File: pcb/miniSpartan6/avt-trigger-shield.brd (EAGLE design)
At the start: 52.1 x 76.2 mm, 20 parts

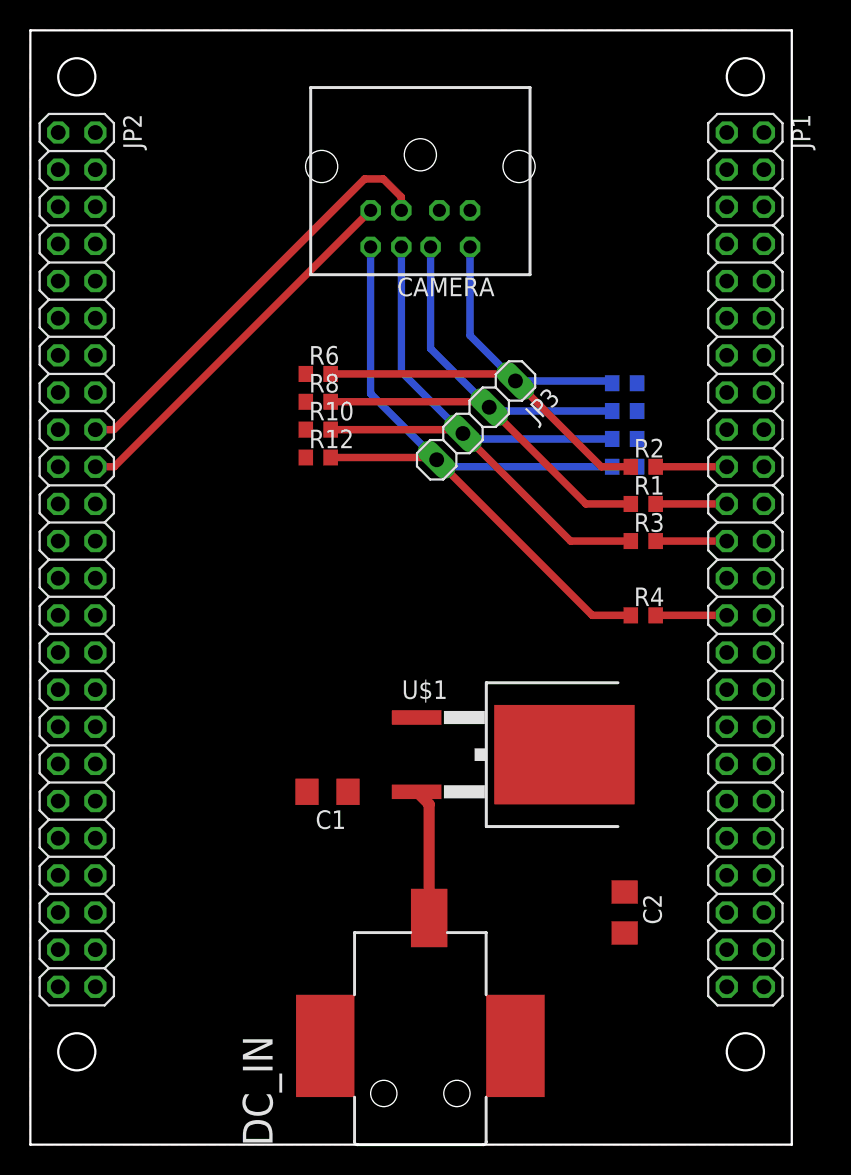
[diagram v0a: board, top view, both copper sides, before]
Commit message: finished avt trigger board
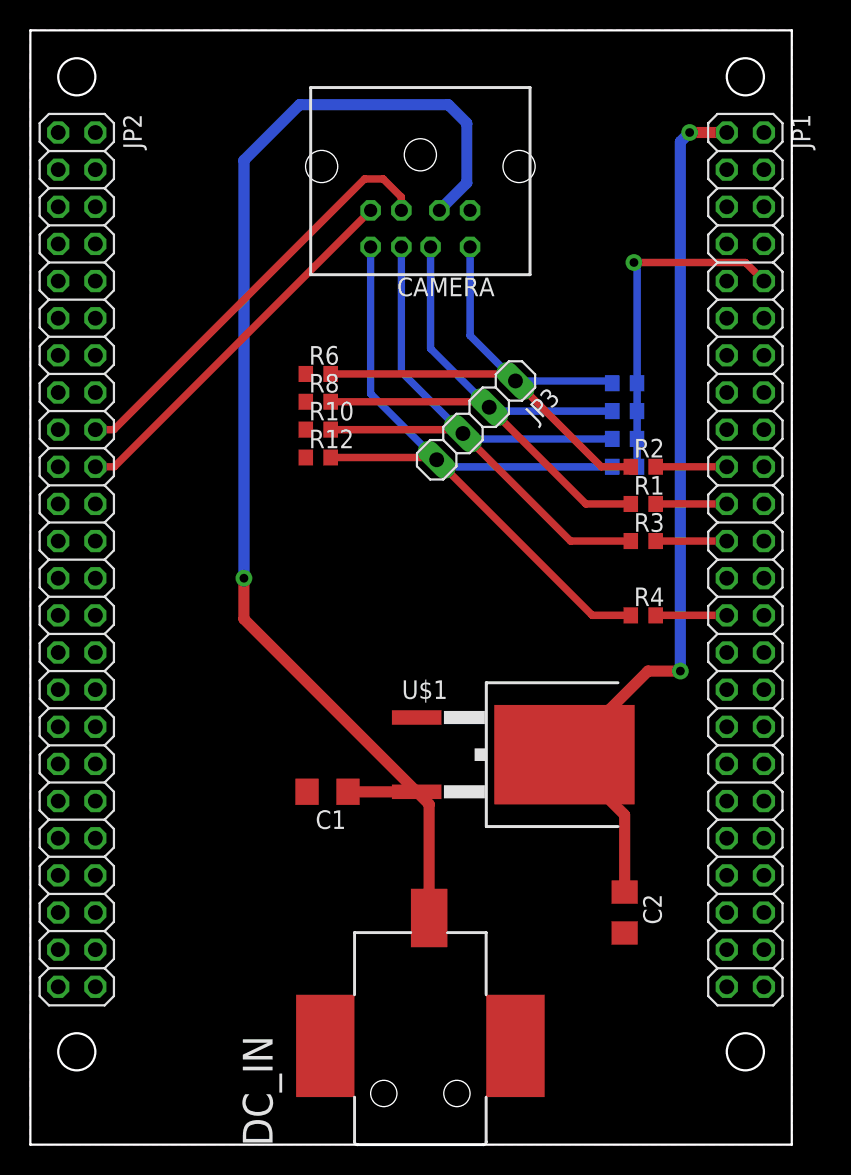
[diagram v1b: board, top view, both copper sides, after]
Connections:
- net 3V3: now also JP1.10
- net GND: now also JP2.47, JP2.48
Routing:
- net VIN: track 8.98 -> 85.8 mm, vias 0 -> 1
- net VCC: track 0.00 -> 61.0 mm, vias 0 -> 2
- net 3V3: track 0.00 -> 23.5 mm, vias 0 -> 1
- added copper zone on layer 16, net GND
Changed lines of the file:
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@@
 <wire x1="27.27" y1="15.5" x2="27.27" y2="23.28" width="0.762" layer="1"/>
 <wire x1="27.27" y1="23.28" x2="26.42" y2="24.13" width="0.762" layer="1"/>
-<wire x1="26.42" y1="24.13" x2="27.97" y2="63.89" width="0" layer="19" extent="1-1"/>
-<wire x1="21.72" y1="24.13" x2="26.42" y2="24.13" width="0" layer="19" extent="1-1"/>
+<wire x1="26.42" y1="24.13" x2="21.72" y2="24.13" width="0.762" layer="1"/>
+<wire x1="26.42" y1="24.13" x2="14.605" y2="35.945" width="0.762" layer="1"/>
+<wire x1="14.605" y1="35.945" x2="14.605" y2="38.735" width="0.762" layer="1"/>
+<via x="14.605" y="38.735" extent="1-16" drill="0.6" diameter="1.15"/>
+<wire x1="14.605" y1="38.735" x2="14.605" y2="67.31" width="0.762" layer="16"/>
+<wire x1="14.605" y1="67.31" x2="18.415" y2="71.12" width="0.762" layer="16"/>
+<wire x1="18.415" y1="71.12" x2="28.575" y2="71.12" width="0.762" layer="16"/>
+<wire x1="28.575" y1="71.12" x2="29.845" y2="69.85" width="0.762" layer="16"/>
+<wire x1="29.845" y1="65.765" x2="27.97" y2="63.89" width="0.762" layer="16"/>
+<wire x1="29.845" y1="69.85" x2="29.845" y2="65.765" width="0.762" layer="16"/>
 </signal>
 <signal name="GND">
@@
 <contactref element="R10" pad="1"/>
 <contactref element="R12" pad="1"/>
+<polygon width="0.762" layer="16" isolate="0.508">
+<vertex x="0" y="76.2"/>
+<vertex x="52.07" y="76.2"/>
+<vertex x="52.07" y="0"/>
+<vertex x="0" y="0"/>
+</polygon>
+<contactref element="JP2" pad="47"/>
+<contactref element="JP2" pad="48"/>
 </signal>
 <signal name="VCC">
@@
 <contactref element="JP1" pad="1"/>
 <contactref element="C2" pad="1"/>
-<wire x1="36.52" y1="26.67" x2="47.625" y2="69.215" width="0" layer="19" extent="1-1"/>
-<wire x1="40.64" y1="17.275" x2="36.52" y2="26.67" width="0" layer="19" extent="1-1"/>
+<wire x1="36.52" y1="26.67" x2="40.64" y2="22.55" width="0.762" layer="1"/>
+<wire x1="40.64" y1="22.55" x2="40.64" y2="17.275" width="0.762" layer="1"/>
+<wire x1="36.52" y1="26.67" x2="42.235" y2="32.385" width="0.762" layer="1"/>
+<wire x1="42.235" y1="32.385" x2="44.45" y2="32.385" width="0.762" layer="1"/>
+<via x="44.45" y="32.385" extent="1-16" drill="0.6" diameter="1.15"/>
+<wire x1="44.45" y1="32.385" x2="44.45" y2="68.58" width="0.762" layer="16"/>
+<wire x1="44.45" y1="68.58" x2="45.085" y2="69.215" width="0.762" layer="16"/>
+<via x="45.085" y="69.215" extent="1-16" drill="0.6" diameter="1.15"/>
+<wire x1="45.085" y1="69.215" x2="47.625" y2="69.215" width="0.762" layer="1"/>
 </signal>
 <signal name="TX">
@@
 <contactref element="R7" pad="2"/>
 <contactref element="R9" pad="2"/>
-<wire x1="41.49" y1="50.165" x2="41.49" y2="52.07" width="0" layer="19" extent="16-16"/>
-<wire x1="41.49" y1="48.26" x2="41.49" y2="50.165" width="0" layer="19" extent="16-16"/>
-<wire x1="41.49" y1="46.355" x2="41.49" y2="48.26" width="0" layer="19" extent="16-16"/>
+<wire x1="41.49" y1="52.07" x2="41.49" y2="50.165" width="0.508" layer="16"/>
+<wire x1="41.49" y1="50.165" x2="41.49" y2="48.26" width="0.508" layer="16"/>
+<wire x1="41.49" y1="48.26" x2="41.49" y2="46.355" width="0.508" layer="16"/>
+<contactref element="JP1" pad="10"/>
+<wire x1="50.165" y1="59.055" x2="48.895" y2="60.325" width="0.508" layer="1"/>
+<wire x1="48.895" y1="60.325" x2="41.275" y2="60.325" width="0.508" layer="1"/>
+<via x="41.275" y="60.325" extent="1-16" drill="0.6" diameter="1.15"/>
+<wire x1="41.275" y1="60.325" x2="41.49" y2="60.11" width="0.508" layer="16"/>
+<wire x1="41.49" y1="60.11" x2="41.49" y2="52.07" width="0.508" layer="16"/>
 </signal>
 </signals>

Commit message: fixed pin assignments
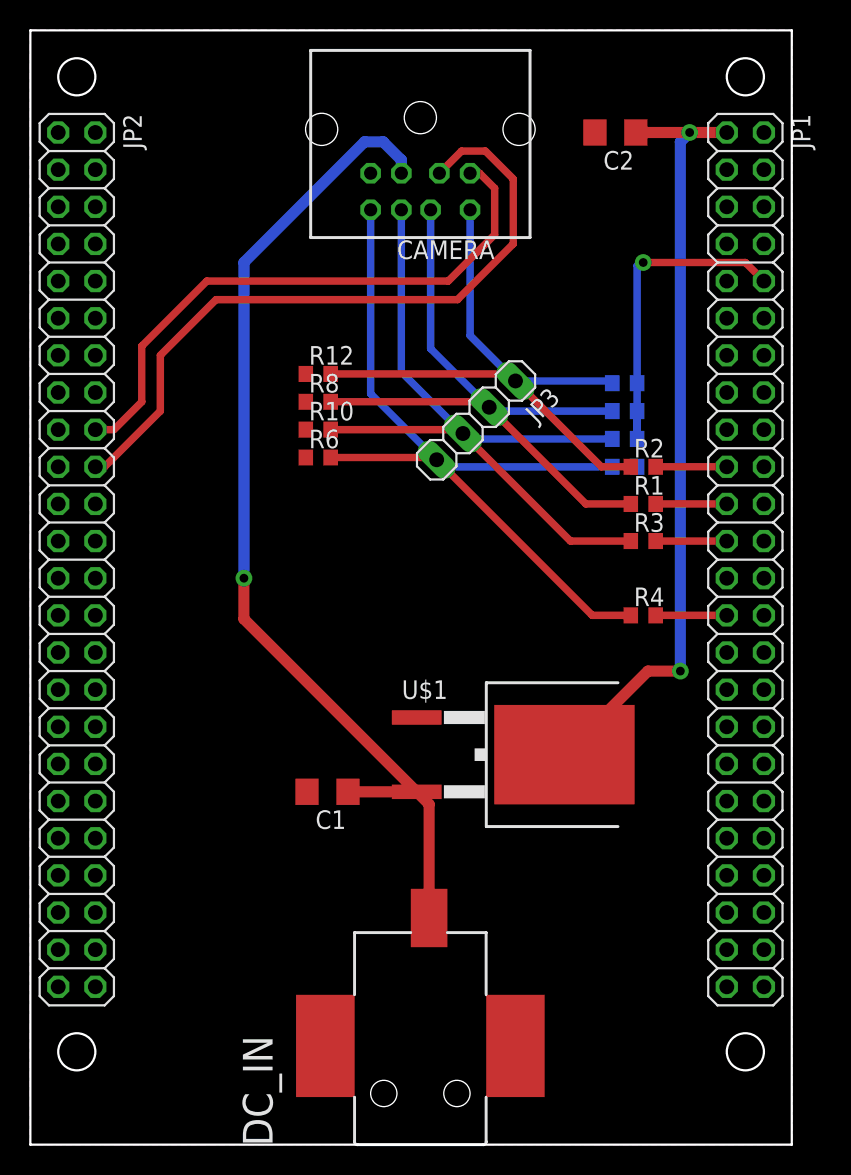
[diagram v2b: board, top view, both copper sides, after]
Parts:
- moved C2 53.3 mm to (40.0, 69.2), turned to 180 degrees
- moved R11 5.72 mm to (40.6, 52.1)
- moved R5 5.72 mm to (40.6, 46.4)
- moved R12 5.71 mm to (19.7, 52.7)
- moved R6 5.71 mm to (19.7, 47.0)
- moved CAMERA 2.54 mm to (26.7, 74.9)
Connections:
- net GND: now also CAMERA.3; no longer CAMERA.5
- net IN1: now also CAMERA.6, JP3.4, R4.1; no longer CAMERA.8, JP3.1, R2.1
- net OUT2: now also CAMERA.8, JP3.1, R2.1; no longer CAMERA.6, JP3.4, R4.1
- net RX: now also CAMERA.5, JP2.18; no longer CAMERA.3, JP2.20
- net TX: now also CAMERA.2, JP2.20; no longer CAMERA.1, JP2.18
- net VIN: now also CAMERA.1; no longer CAMERA.2
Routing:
- net TX: track 29.5 -> 48.0 mm
- net IN1: track 40.3 -> 56.2 mm
- net VIN: track 85.8 -> 70.4 mm
- net RX: track 26.1 -> 39.7 mm
- net OUT2: track 53.6 -> 42.8 mm
- net VCC: track 61.0 -> 53.6 mm
- net IN2: track 44.6 -> 47.1 mm
- net OUT1: track 48.5 -> 51.1 mm
